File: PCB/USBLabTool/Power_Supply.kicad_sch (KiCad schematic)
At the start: 64 parts, among them J2 Conn_01x01, J25 T_N5V, J3 T_P5V, P2 USB_C_Plug_USB2.0, Q1 IRLML6402TRPBF, U10 Opamp_Quad, U11 LTC1983ES6-5#TRPBF, U12 DG403, U14 r1283, U15 XC6206PxxxMR, U16 XC6206PxxxMR, U9 Opamp_Quad

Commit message: update components and wiring
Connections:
- net +12VA: no longer D7.2 (A)
- net +5V: now also D7.2 (A)
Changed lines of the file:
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@@
 			)
 		)
-		(property "Value" "+12VA"
-			(at 79.502 122.936 0)
+		(property "Value" "+5V"
+			(at 83.058 123.19 0)
 			(effects
 				(font

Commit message: change USB design and MCU
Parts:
- removed C1: 10u, Capacitor_SMD:C_0603_1608Metric_Pad1.08x0.95mm_HandSolder, symbol Device:C
- removed C2: 1.5u, Capacitor_SMD:C_0603_1608Metric_Pad1.08x0.95mm_HandSolder, symbol Device:C
- removed C3: 1m, Capacitor_THT:CP_Radial_D10.0mm_P5.00mm, symbol Device:C
- removed C57, C58, C59: 100n, Capacitor_SMD:C_0603_1608Metric_Pad1.08x0.95mm_HandSolder, symbol Device:C
- removed J2: Conn_01x01, Connector_PinHeader_2.54mm:PinHeader_1x01_P2.54mm_Vertical, symbol Connector_Generic:Conn_01x01
- removed J3: T_P5V, Connector_PinHeader_2.54mm:PinHeader_1x01_P2.54mm_Vertical, symbol Connector_Generic:Conn_01x01
- removed P2: USB_C_Plug_USB2.0, Connector_USB:USB_C_Receptacle_JAE_DX07S016JA1R1500, symbol Connector:USB_C_Plug_USB2.0
- removed Q1: IRLML6402TRPBF, Package_TO_SOT_SMD:SOT-23-3, symbol dk_Transistors-FETs-MOSFETs-Single:IRLML6402TRPBF
- removed R1: 27k, Resistor_SMD:R_0603_1608Metric_Pad0.98x0.95mm_HandSolder, symbol Device:R
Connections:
- net +5V: no longer C33.1, D8.2 (A), L3.1, U14.11 (PVcc), U14.5 (CE), U14.8 (Vcc)
- new net +5VCLEAN: C33.1, D8.2 (A), L3.1, U14.11 (PVcc), U14.5 (CE), U14.8 (Vcc)
- no-connect marks 3 -> 0
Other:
- note removed: "USB Soft Start Schematic"
- note removed: "Vout"

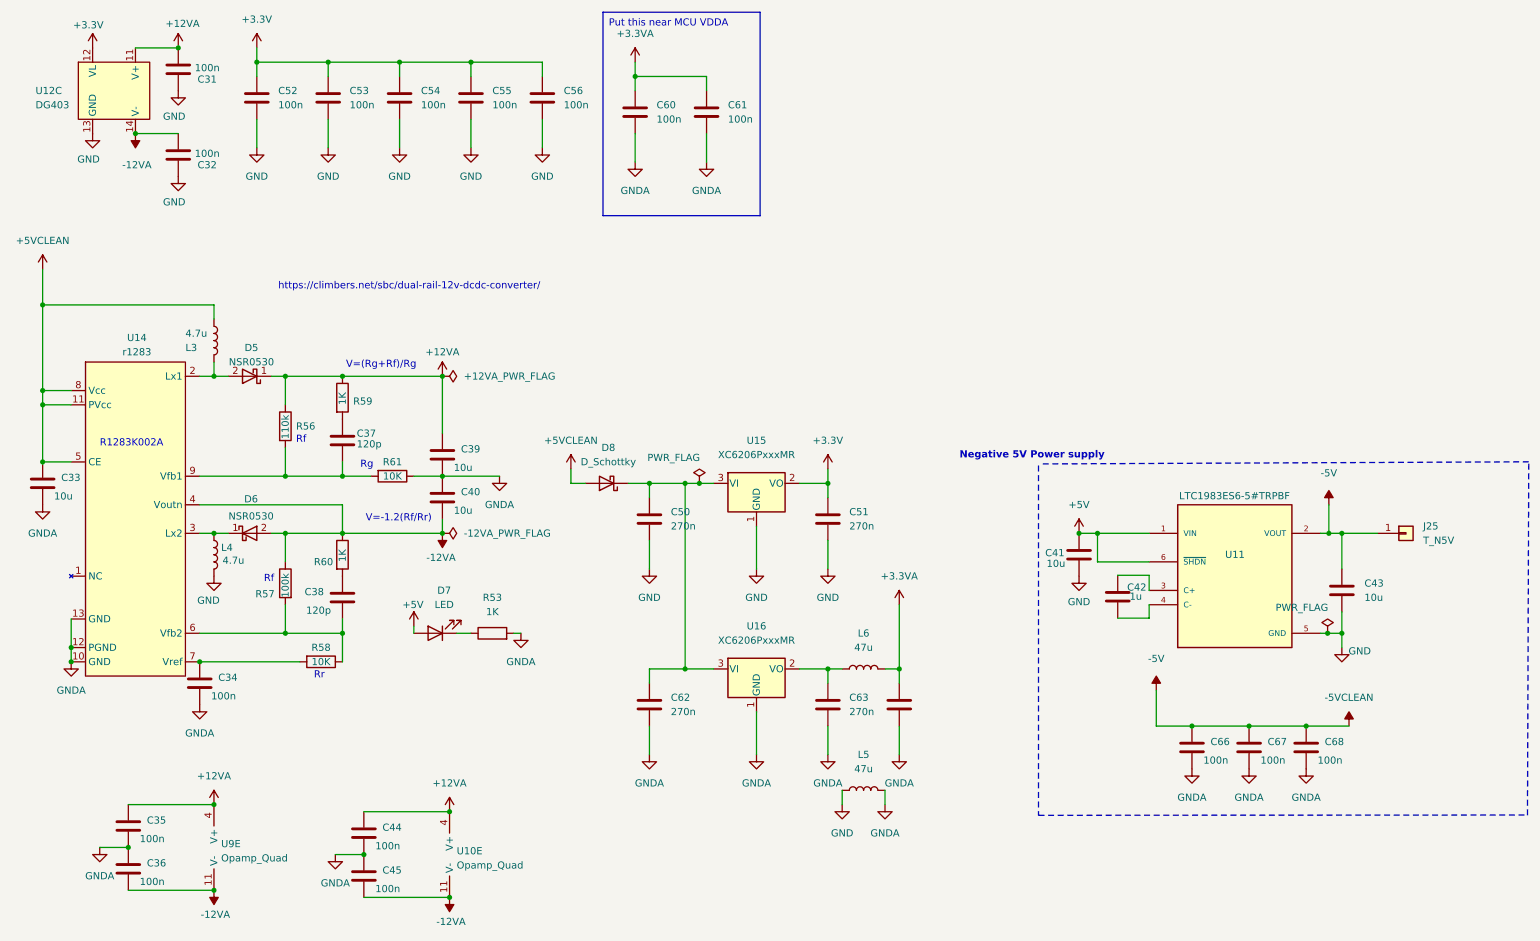
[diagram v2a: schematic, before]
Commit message: update MCU and USB, fix some footprints
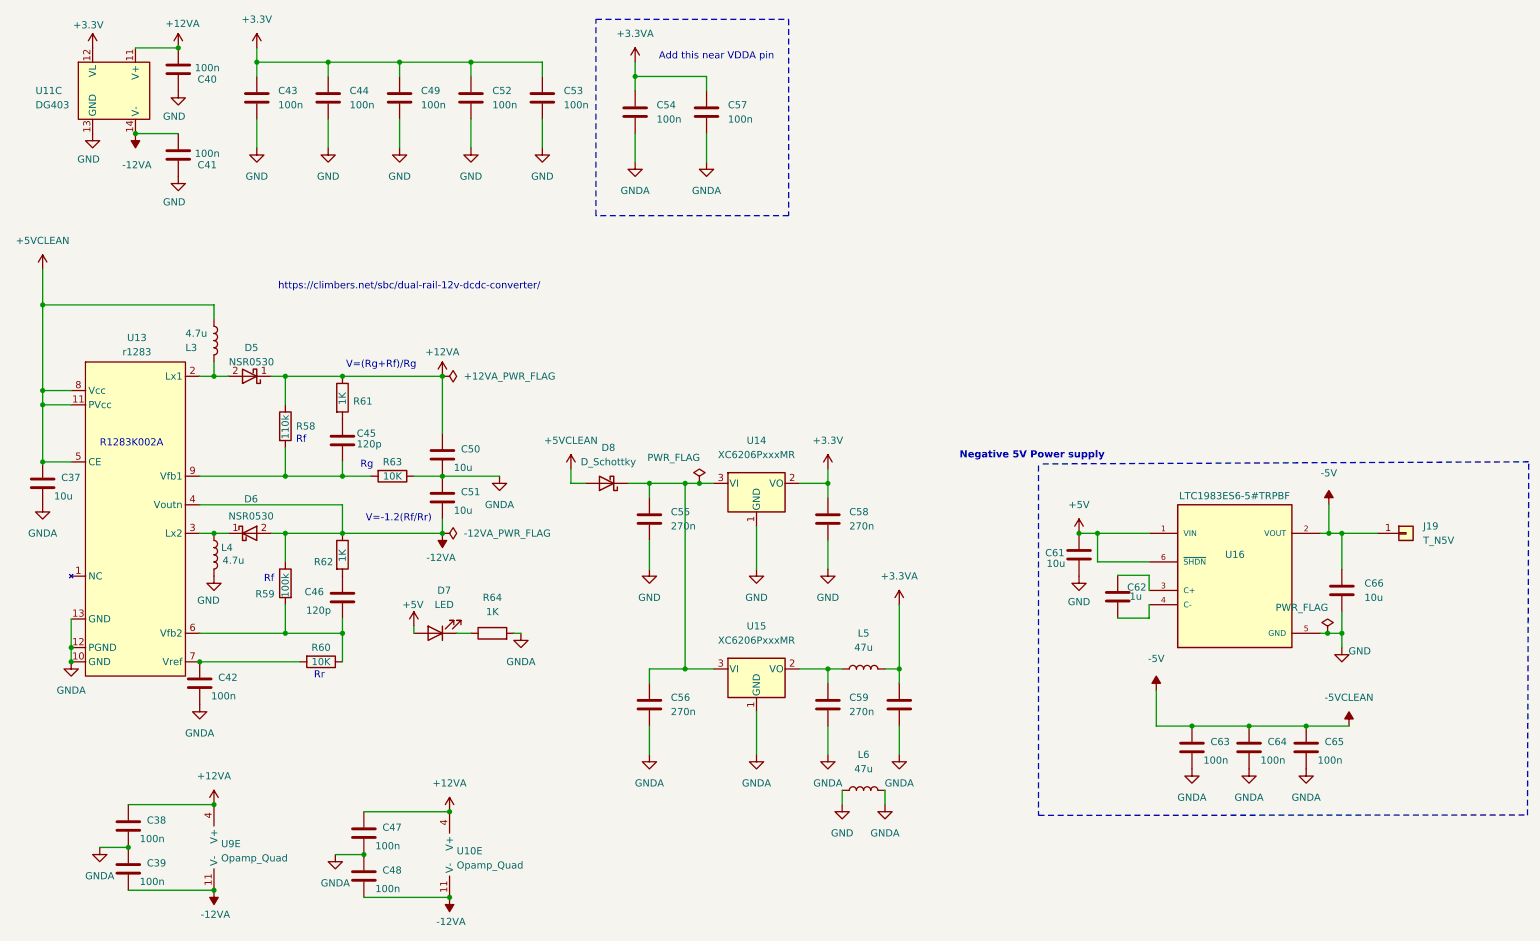
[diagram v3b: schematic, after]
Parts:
- C42: renamed from C34; footprint Capacitor_SMD:C_0603_1608Metric_Pad1.08x0.95mm_HandSolder -> Capacitor_SMD:C_0201_0603Metric_Pad0.64x0.40mm_HandSolder
- renumbered C33 to C37, C35 to C38, C36 to C39, C31 to C40, C32 to C41, C52 to C43, C53 to C44, C37 to C45, C38 to C46, C44 to C47, C45 to C48, C54 to C49, C39 to C50, C40 to C51, C55 to C52, C56 to C53, C60 to C54, C50 to C55, C62 to C56, C61 to C57, C51 to C58, C63 to C59, C64 to C60, C41 to C61, C42 to C62, C66 to C63, C67 to C64, C68 to C65, C43 to C66, J25 to J19, L6 to L5, L5 to L6, R56 to R58, R57 to R59, R58 to R60, R59 to R61, R60 to R62, R61 to R63, R53 to R64, U12 to U11, U14 to U13, U15 to U14, U16 to U15, U11 to U16
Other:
- note added: "Add this near VDDA pin"

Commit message: Fixed up footprints
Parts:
- L3, L4: footprint footprints:IND_TAIYO_NRH2410_TAY -> userfp:IND_TAIYO_NRH2410_TAY
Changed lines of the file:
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@@
 			)
 		)
-		(property "Footprint" "footprints:IND_TAIYO_NRH2410_TAY"
+		(property "Footprint" "userfp:IND_TAIYO_NRH2410_TAY"
 			(at 49.53 76.2 0)
 			(effects
@@
 			)
 		)
-		(property "Footprint" "footprints:IND_TAIYO_NRH2410_TAY"
+		(property "Footprint" "userfp:IND_TAIYO_NRH2410_TAY"
 			(at 49.53 114.3 0)
 			(effects

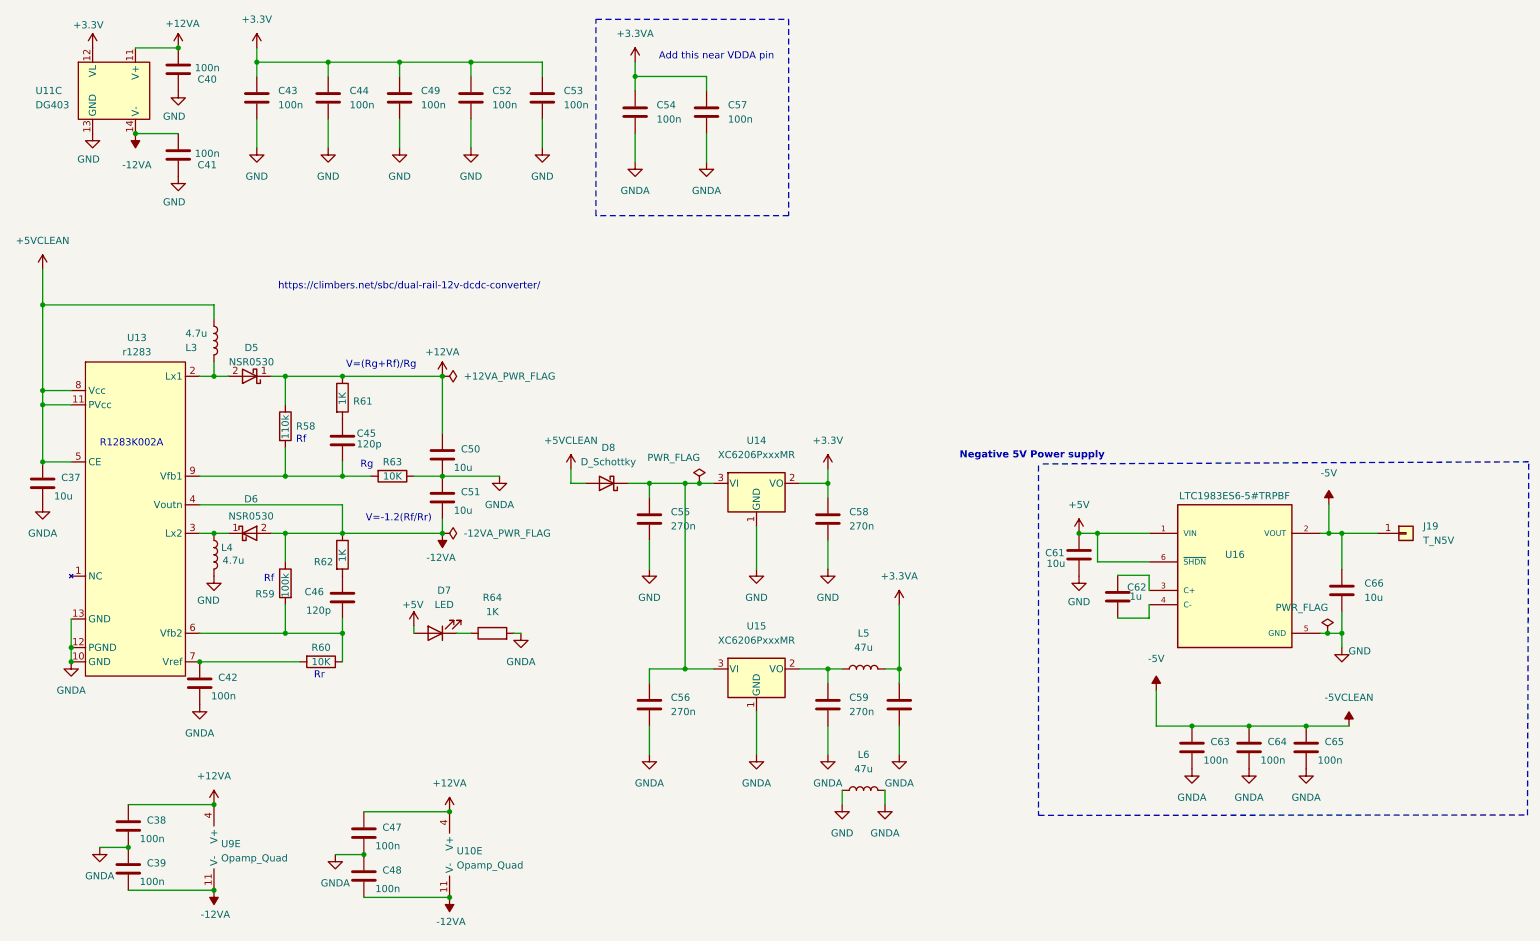
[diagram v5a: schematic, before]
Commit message: change 3.3V regulator
Using ST1L05APU33R instead of ST1L05CPU33R for simplicity and save of sanity
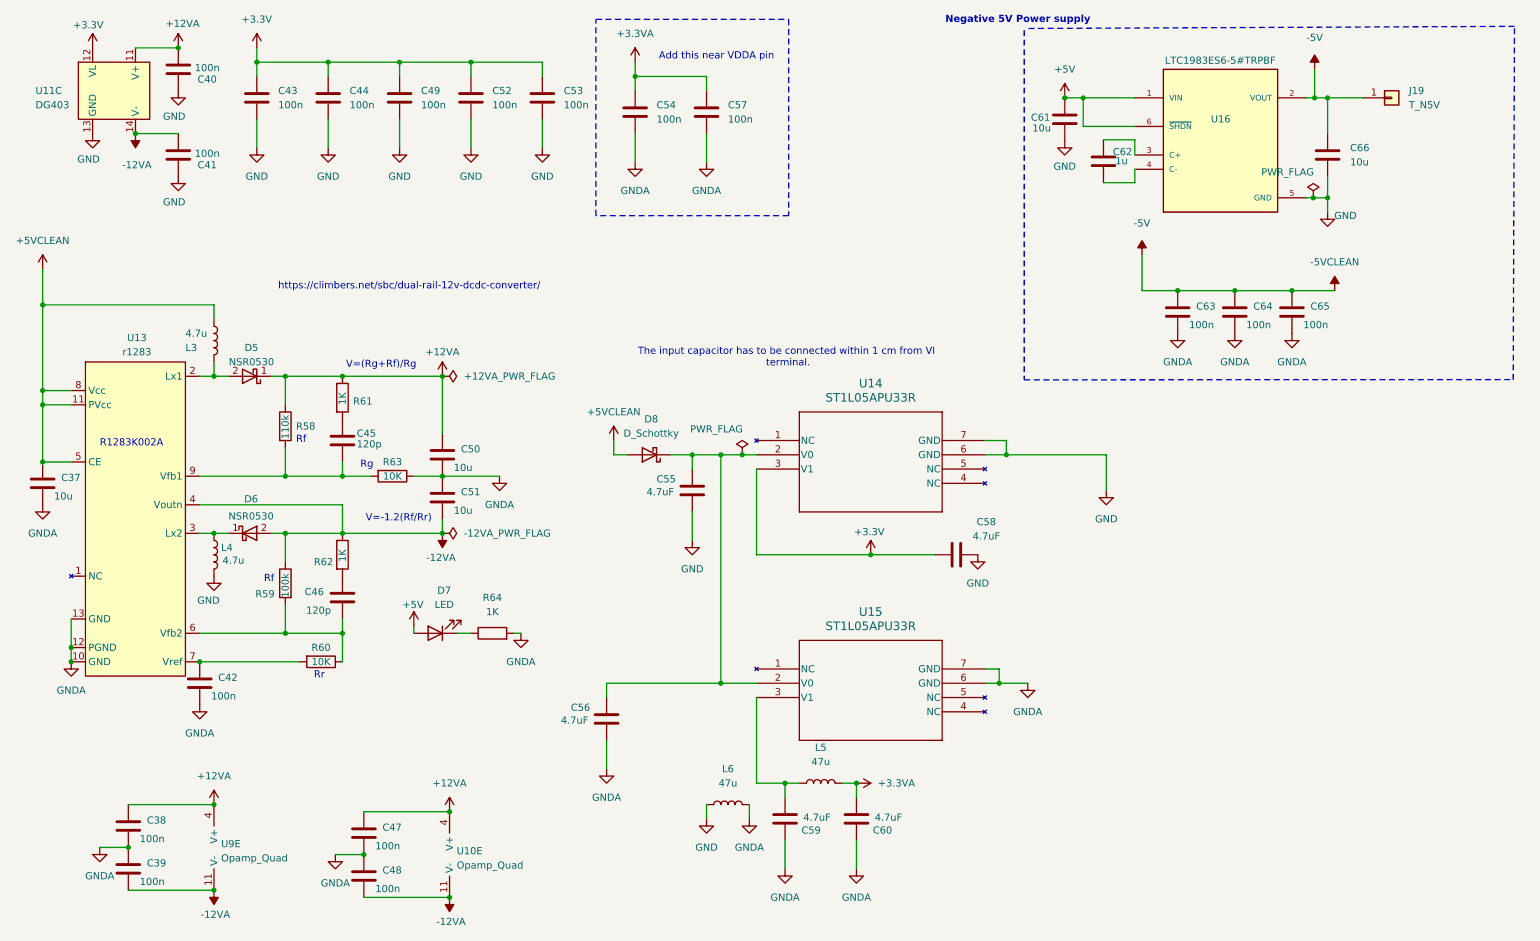
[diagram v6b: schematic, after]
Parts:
- removed U14, U15: XC6206PxxxMR, Package_TO_SOT_SMD:SOT-23-3, symbol Regulator_Linear:XC6206PxxxMR
- added U14, U15: ST1L05APU33R, DFN_5APU33R_STM, symbol ST1L05APU33R:ST1L05APU33R
- C55, C56, C58, C59, C60: value 270n -> 4.7uF
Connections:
- net +3.3V: now also C58.2, U14.3 (V1); no longer C58.1
- net +3.3VA: now also C60.2; no longer C60.1
- net GND: now also C58.1, U14.6 (GND), U14.7 (GND); no longer C58.2
- net GNDA: now also C59.1, C60.1, U15.6 (GND), U15.7 (GND); no longer C59.2, C60.2
- net at L5.1: now also C59.2, U15.3 (V1); no longer C59.1
- net at C55.1, C56.1, D8.1 (K): now also U14.2 (V0), U15.2 (V0)
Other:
- note added: "The input capacitor has to be connected within 1 cm from VI terminal."
- moved on the sheet: C55, C61, C62, C63, C64, C65, C66, D8, J19, U16

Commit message: Update Power_Supply.kicad_sch
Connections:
- net +3.3V: now also U14.2 (V0); no longer U14.3 (V1)
- net at C59.2, L5.1: now also U15.2 (V0); no longer U15.3 (V1)
- net at C55.1, C56.1, D8.1 (K): now also U14.3 (V1), U15.3 (V1); no longer U14.2 (V0), U15.2 (V0)
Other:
- moved on the sheet: C55, C56, C58, C59, C60, D8, L5, L6, U15
